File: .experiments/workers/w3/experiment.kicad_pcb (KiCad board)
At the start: 2 copper layers, 140 x 90 mm, 39 parts, among them J1 USB_C, J2 Output, J3 Debug, Q1 FS8205A, U1 USBLC6-2SC6, U2 BQ24072, U3 HY2113-KB5B, U4 MT3608, U5 AP2112K-3.3, U6 LN61CN3302MR-G

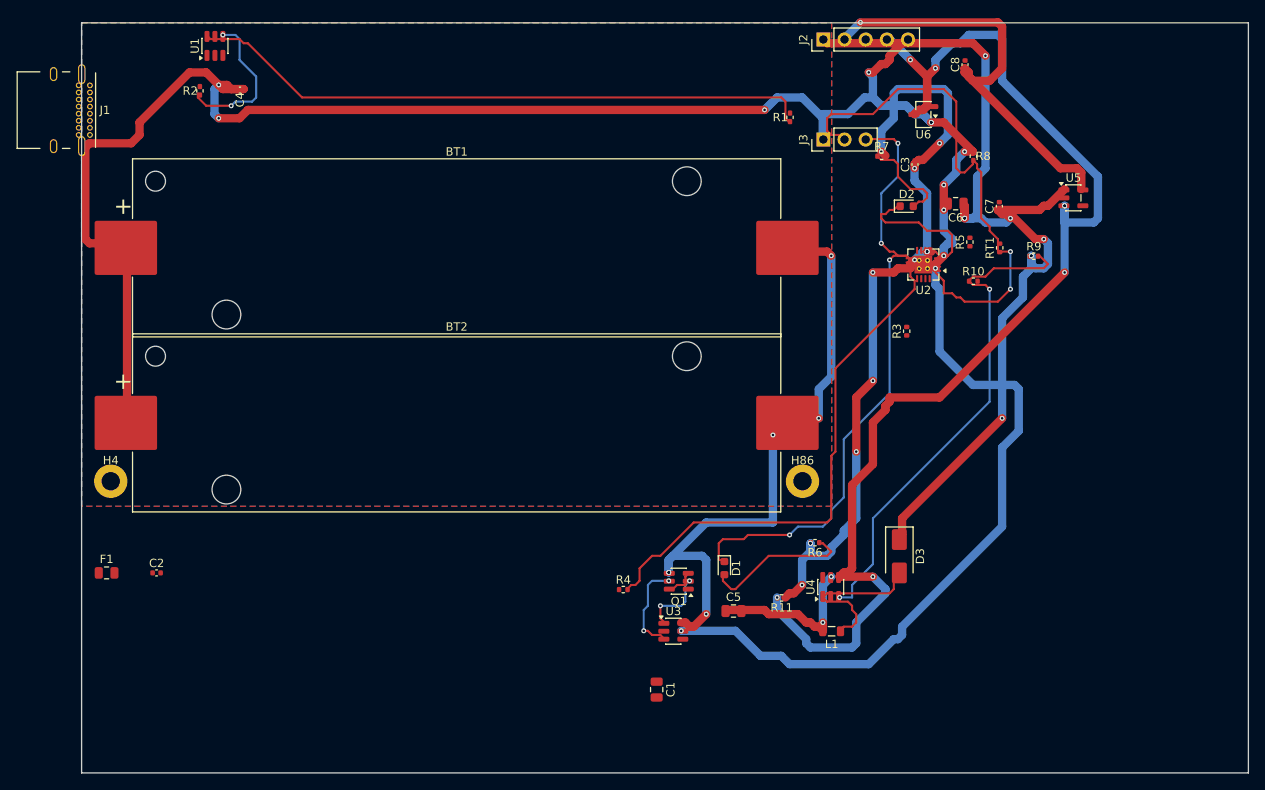
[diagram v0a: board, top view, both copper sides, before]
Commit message: 35-round experiment: best score 25.33, improved routing params
Router and conflict resolution tuning from autonomous optimization loop.
Best config: clearance=0.2051mm, cooling_factor=0.9735, existing_trace_cost=200.0

Co-Authored-By: Claude Opus 4.6 <noreply@anthropic.com>
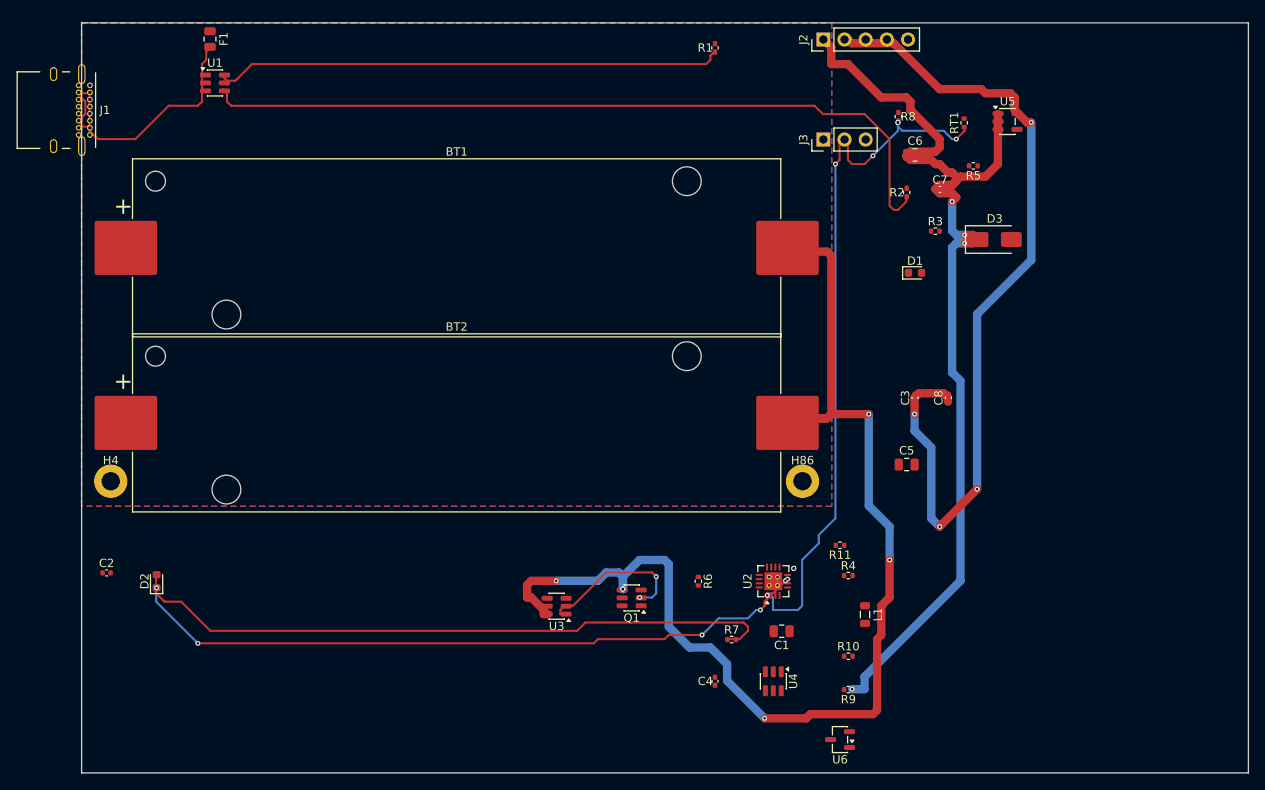
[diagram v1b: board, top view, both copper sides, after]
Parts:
- moved D2 100.6 mm to (9.00, 67.0), turned to 90 degrees
- moved C4 91.0 mm to (76.0, 79.0), turned to 90 degrees
- moved R2 85.7 mm to (99.0, 20.4)
- moved U6 75.7 mm to (91.0, 86.0)
- moved F1 65.2 mm to (15.4, 1.94), turned to -90 degrees
- moved R7 60.7 mm to (78.0, 74.0)
- moved R9 56.6 mm to (92.0, 80.0), turned to 180 degrees
- moved R10 47.4 mm to (92.0, 76.0)
- moved D1 42.2 mm to (100.0, 30.0), turned to 0 degrees
- moved U2 42.0 mm to (83.0, 67.0), turned to 90 degrees
- moved C8 40.0 mm to (104.0, 45.0)
- moved D3 39.7 mm to (109.6, 26.0), turned to 0 degrees
- moved C3 28.0 mm to (100.0, 45.0)
- moved C5 27.2 mm to (99.0, 53.0)
- moved R4 27.1 mm to (92.0, 66.3)
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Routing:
- net /VBAT: track 293.0 -> 0.00 mm, vias 14 -> 0
- net /EN: track 149.0 -> 0.00 mm, vias 8 -> 0
- net /VSYS: track 93.0 -> 0.00 mm, vias 12 -> 2
- net Net-(R2-Pad1): track 18.4 -> 94.2 mm, vias 2 -> 0
- net /CHG_N: track 75.4 -> 0.00 mm, vias 4 -> 0
- net /CELL_NEG: track 75.5 -> 144.0 mm
- net Net-(D2-A): track 11.2 -> 78.9 mm
- net Net-(D2-K): track 18.7 -> 82.5 mm, vias 0 -> 6
- net Net-(U2-ILIM): track 62.7 -> 0.00 mm
- net Net-(U4-FB): track 60.0 -> 0.00 mm, vias 2 -> 0
- net /3V3: track 52.5 -> 102.2 mm, vias 2 -> 4
- net Net-(F1-Pad2): track 0.00 -> 33.6 mm
- net /NTC_SENSE: track 62.8 -> 85.6 mm, vias 2 -> 8
- net Net-(D3-A): track 19.7 -> 0.00 mm
- net /VSYS_BOOST: track 19.4 -> 0.00 mm, vias 2 -> 0
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
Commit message: 45-round experiment: best score 25.66, all nets routed (26/26)
Fixed A* performance by increasing max_search from 100k->500k to handle
high trace costs (100.0) without timing out. Kept high cost + coarse grid
(0.5mm) to prevent shorts while still routing efficiently.

Best config: edge_margin=5.7493mm, cooling_factor=0.9764, existing_trace_cost=200, max_rips=8

Co-Authored-By: Claude Opus 4.6 <noreply@anthropic.com>
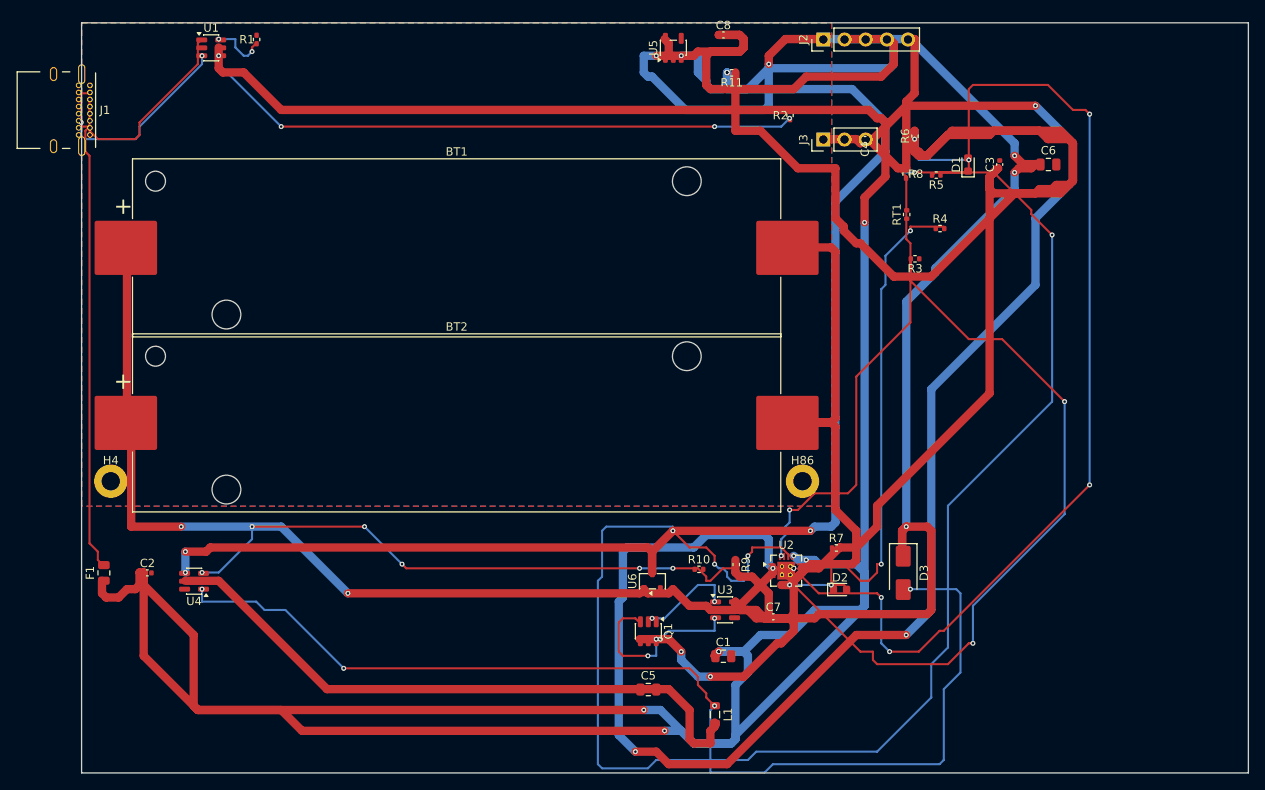
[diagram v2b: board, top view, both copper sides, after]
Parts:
- moved D2 82.0 mm to (91.0, 68.0), turned to 0 degrees
- moved U4 70.5 mm to (13.5, 67.0), turned to 180 degrees
- moved C4 67.4 mm to (94.0, 14.0), turned to 180 degrees
- moved F1 65.3 mm to (2.67, 66.0), turned to 90 degrees
- moved R6 59.4 mm to (100.0, 13.6), turned to 90 degrees
- moved R11 58.2 mm to (78.0, 6.00)
- moved C7 55.0 mm to (83.0, 71.3)
- moved R1 55.0 mm to (21.0, 2.00)
- moved C8 51.2 mm to (77.0, 1.46), turned to 0 degrees
- moved R4 43.1 mm to (103.0, 24.7)
- moved D3 41.5 mm to (98.6, 66.0), turned to -90 degrees
- moved C5 41.1 mm to (68.0, 80.0)
- moved U5 41.1 mm to (71.0, 3.00), turned to 90 degrees
- moved C3 29.8 mm to (110.2, 17.0)
- moved U6 29.5 mm to (68.5, 67.0), turned to 90 degrees
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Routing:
- net /VBUS: track 0.00 -> 395.4 mm, vias 0 -> 6
- net /VBAT: track 0.00 -> 328.9 mm, vias 0 -> 6
- net /EN: track 0.00 -> 197.8 mm, vias 0 -> 8
- net /VSYS: track 0.00 -> 196.9 mm
- net Net-(U2-TMR): track 0.00 -> 181.9 mm, vias 0 -> 4
- net /CHG_N: track 0.00 -> 134.5 mm, vias 0 -> 6
- net Net-(D3-A): track 0.00 -> 133.9 mm, vias 0 -> 4
- net Net-(D2-K): track 82.5 -> 5.71 mm, vias 6 -> 2
- net /VSYS_BOOST: track 0.00 -> 75.8 mm
- net Net-(D2-A): track 78.9 -> 6.41 mm, vias 0 -> 1
- net Net-(U4-FB): track 0.00 -> 70.8 mm, vias 0 -> 6
- net Net-(U2-ILIM): track 0.00 -> 57.7 mm, vias 0 -> 2
- net Net-(R1-Pad1): track 60.9 -> 6.83 mm, vias 0 -> 2
- net Net-(U2-ISET): track 0.00 -> 44.8 mm, vias 0 -> 2
- net /5V: track 125.0 -> 169.2 mm, vias 4 -> 6
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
